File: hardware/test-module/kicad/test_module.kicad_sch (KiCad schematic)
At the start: 13 parts, among them J1 Barrel_Jack_12V, M1 ERM_Motor, M2 Stepper_4wire, M3 Servo_3pin, U1 D24V22F5_Buck, U2 Pi_Pico, U3 DRV2605L_Breakout, U4 DRV8871_Breakout, U5 DRV8825_Carrier

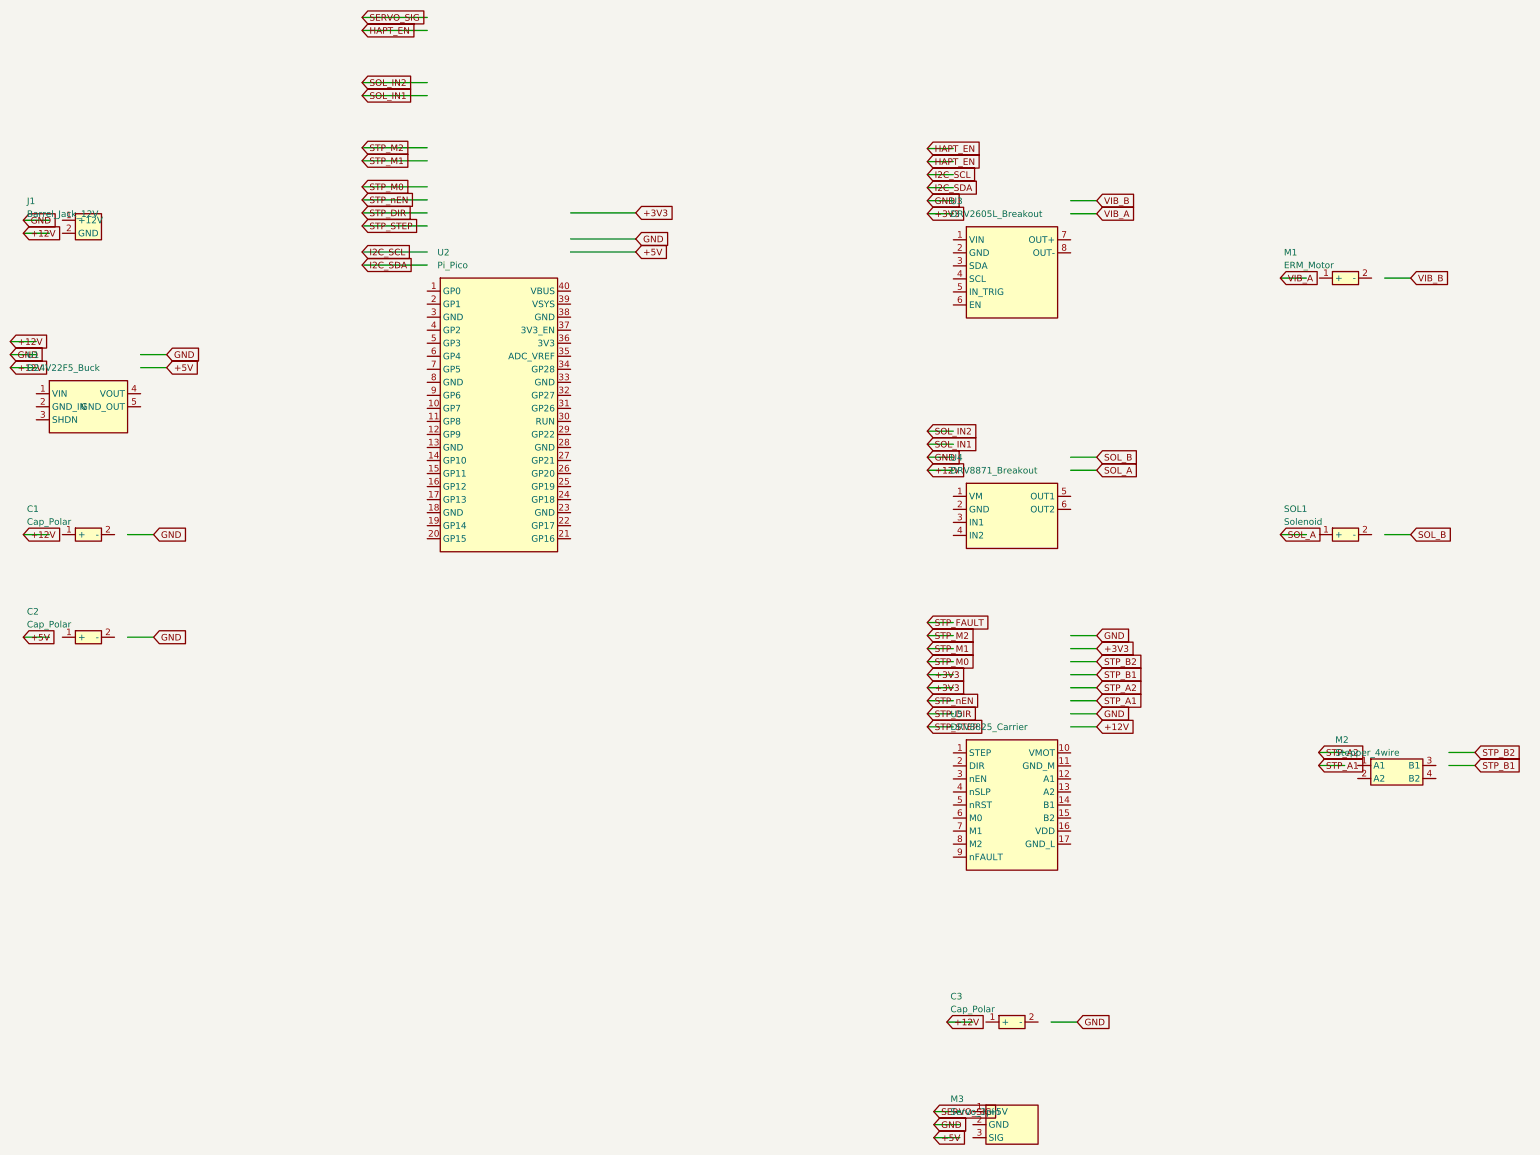
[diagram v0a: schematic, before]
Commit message: Address PR review: smooth servo, Pico W, fix schematic alignment, add shunt regulator
Agent-Logs-Url: https://github.com/vertical-cloud-lab/powder-doser/sessions/35e0fe52-25cf-4560-81b1-879b81744dff

Co-authored-by: swcharles <185848910+swcharles@users.noreply.github.com>
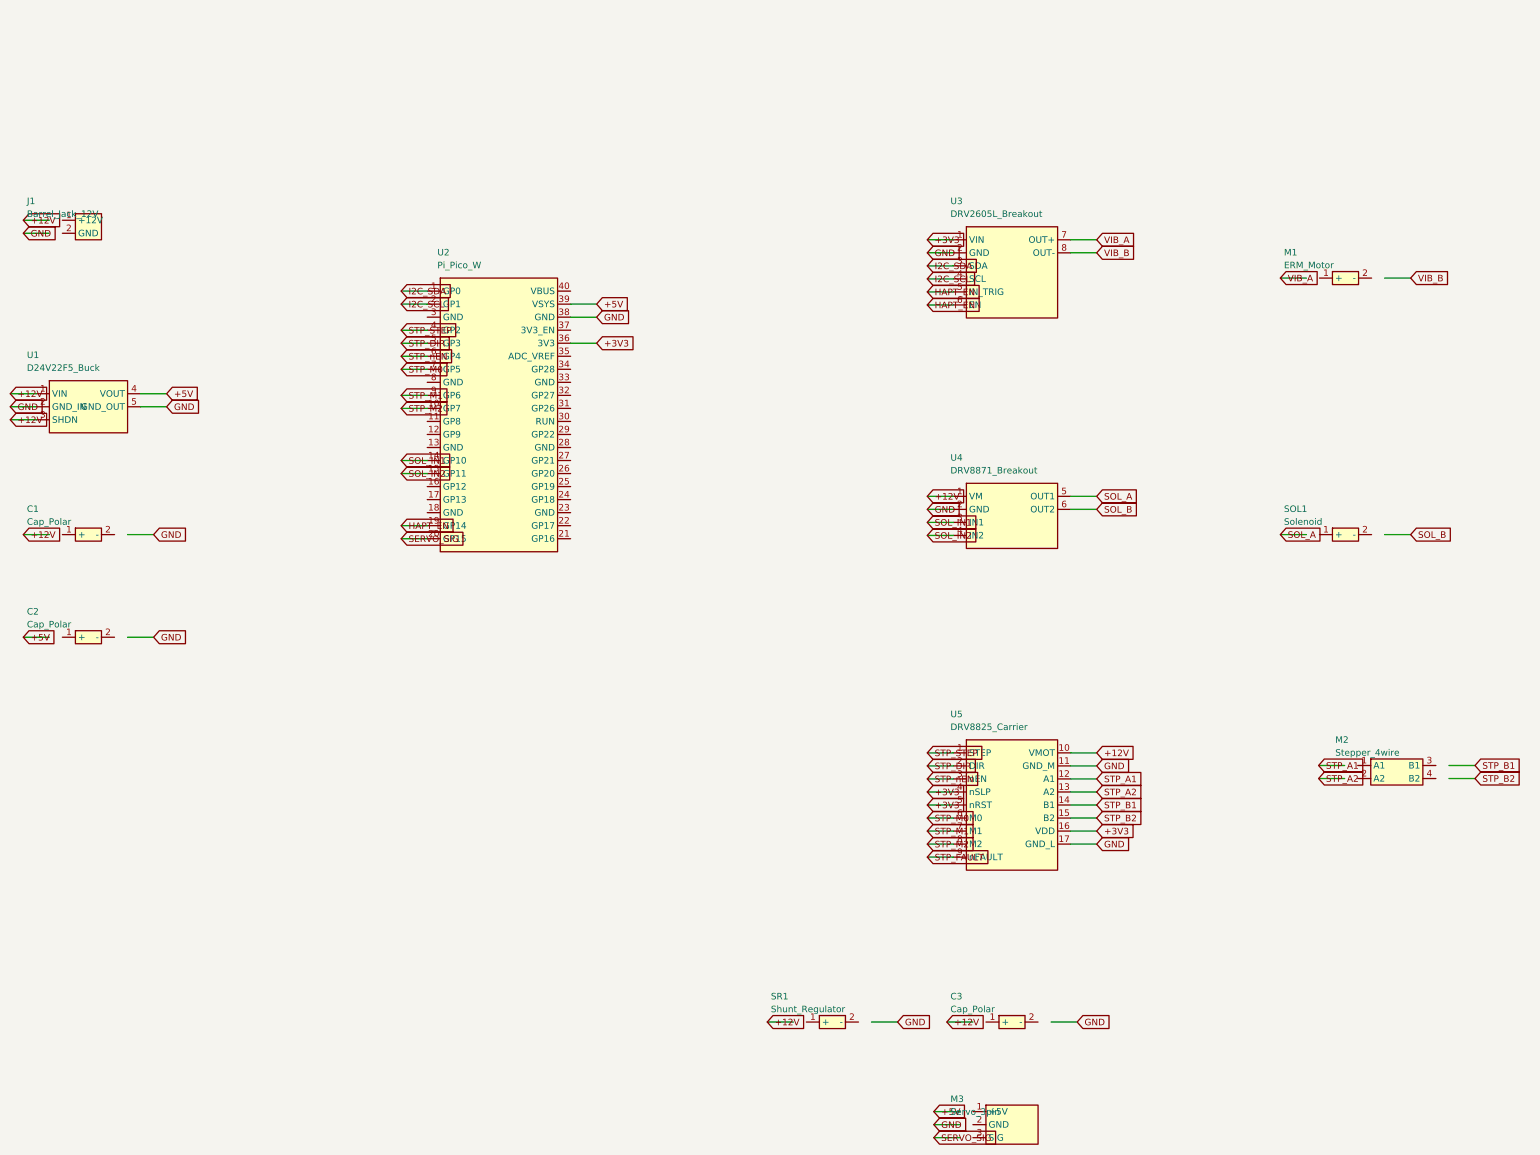
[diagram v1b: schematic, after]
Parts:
- removed U2: Pi_Pico, symbol test_module:Pi_Pico
- added SR1: Shunt_Regulator, symbol test_module:Shunt_Regulator
- added U2: Pi_Pico_W, symbol test_module:Pi_Pico_W
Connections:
- net +12V: now also U1.1 (VIN), U1.3 (SHDN), U4.1 (VM), U5.10 (VMOT)
- net +3V3: now also U3.1 (VIN), U5.16 (VDD), U5.4 (nSLP), U5.5 (nRST), U2.36 (3V3)
- net +5V: now also U1.4 (VOUT), U2.39 (VSYS)
- net GND: now also U1.2 (GND_IN), U1.5 (GND_OUT), U3.2 (GND), U4.2 (GND), U5.11 (GND_M), U5.17 (GND_L), U2.38 (GND)
- net HAPT_EN: now also U3.5 (IN_TRIG), U3.6 (EN), U2.19 (GP14)
- net I2C_SCL: now also U3.4 (SCL), U2.2 (GP1)
- net I2C_SDA: now also U3.3 (SDA), U2.1 (GP0)
- net SERVO_SIG: now also U2.20 (GP15)
- net SOL_A: now also U4.5 (OUT1)
- net SOL_B: now also U4.6 (OUT2)
- net SOL_IN1: now also U4.3 (IN1), U2.14 (GP10)
- net SOL_IN2: now also U4.4 (IN2), U2.15 (GP11)
- net STP_A1: now also U5.12 (A1)
- net STP_A2: now also U5.13 (A2)
- net STP_B1: now also U5.14 (B1)
- net STP_B2: now also U5.15 (B2)
- net STP_DIR: now also U5.2 (DIR), U2.5 (GP3)
- net STP_FAULT: now also U5.9 (nFAULT)
- net STP_M0: now also U5.6 (M0), U2.7 (GP5)
- net STP_M1: now also U5.7 (M1), U2.9 (GP6)
- net STP_M2: now also U5.8 (M2), U2.10 (GP7)
- net STP_STEP: now also U5.1 (STEP), U2.4 (GP2)
- net STP_nEN: now also U5.3 (nEN), U2.6 (GP4)
- net VIB_A: now also U3.7 (OUT+)
- net VIB_B: now also U3.8 (OUT-)

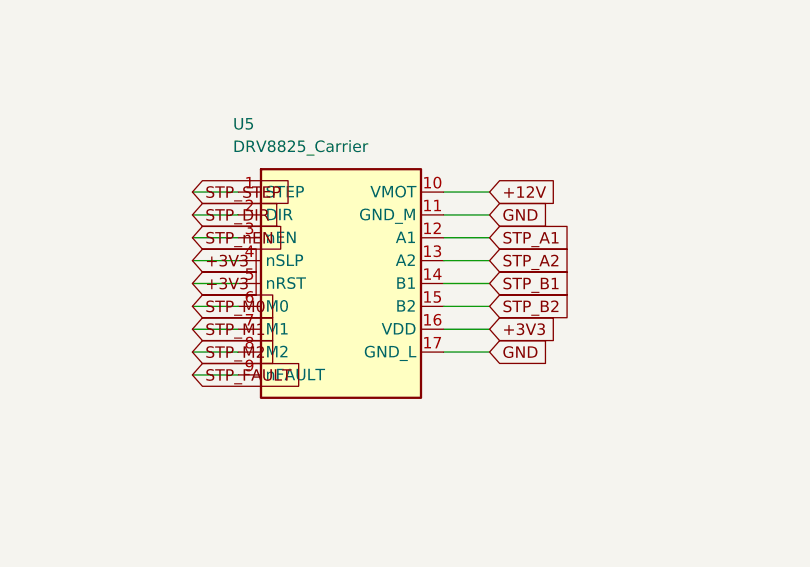
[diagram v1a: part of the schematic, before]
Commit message: DRV8825: 8-pin Pololu #2133 layout (no VDD); document Tic T500 omission
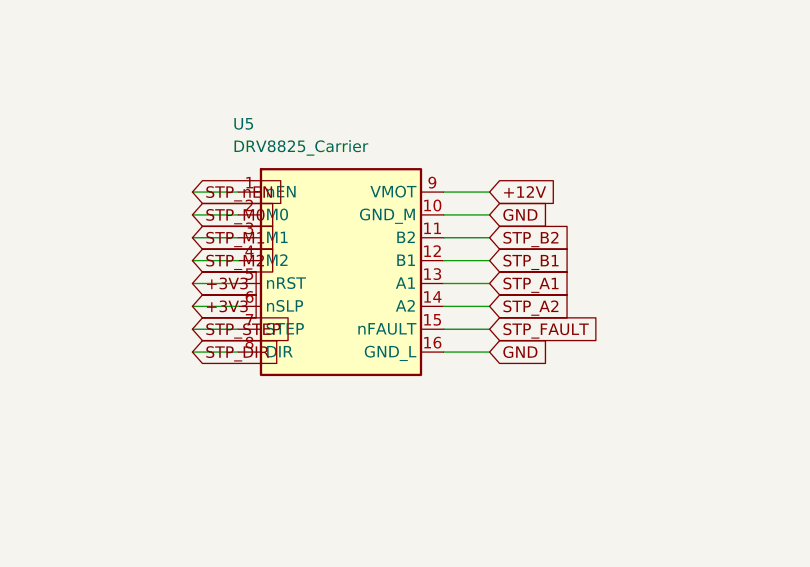
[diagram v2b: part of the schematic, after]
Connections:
- net +12V: now also U5.9 (VMOT); no longer U5.10 (VMOT)
- net +3V3: now also U5.6 (nSLP); no longer U5.16 (VDD), U5.4 (nSLP)
- net GND: now also U5.10 (GND_M), U5.16 (GND_L); no longer U5.11 (GND_M), U5.17 (GND_L)
- net STP_A1: now also U5.13 (A1); no longer U5.12 (A1)
- net STP_A2: now also U5.14 (A2); no longer U5.13 (A2)
- net STP_B1: now also U5.12 (B1); no longer U5.14 (B1)
- net STP_B2: now also U5.11 (B2); no longer U5.15 (B2)
- net STP_DIR: now also U5.8 (DIR); no longer U5.2 (DIR)
- net STP_FAULT: now also U5.15 (nFAULT); no longer U5.9 (nFAULT)
- net STP_M0: now also U5.2 (M0); no longer U5.6 (M0)
- net STP_M1: now also U5.3 (M1); no longer U5.7 (M1)
- net STP_M2: now also U5.4 (M2); no longer U5.8 (M2)
- net STP_STEP: now also U5.7 (STEP); no longer U5.1 (STEP)
- net STP_nEN: now also U5.1 (nEN); no longer U5.3 (nEN)
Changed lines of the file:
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@@
   )
+)
+(wire (pts (xy 198.57 157.78) (xy 193.48999999999998 157.78))
+  (stroke (width 0) (type default)) (stroke (width 0) (type default))
+)
+(global_label "STP_STEP" (shape input) (at 193.48999999999998 157.78 180) (fields_autoplaced)
+  (effects (font (size 1.27 1.27)) (justify left))
+)
+(wire (pts (xy 198.57 160.32) (xy 193.48999999999998 160.32))
+  (stroke (width 0) (type default)) (stroke (width 0) (type default))
+)
+(global_label "STP_DIR" (shape input) (at 193.48999999999998 160.32 180) (fields_autoplaced)
+  (effects (font (size 1.27 1.27)) (justify left))
 )
 (wire (pts (xy 198.57 142.54) (xy 193.48999999999998 142.54))
   (stroke (width 0) (type default)) (stroke (width 0) (type default))
 )
-(global_label "STP_STEP" (shape input) (at 193.48999999999998 142.54 180) (fields_autoplaced)
+(global_label "STP_nEN" (shape input) (at 193.48999999999998 142.54 180) (fields_autoplaced)
   (effects (font (size 1.27 1.27)) (justify left))
 )
-(wire (pts (xy 198.57 145.08) (xy 193.48999999999998 145.08))
+(wire (pts (xy 198.57 155.24) (xy 193.48999999999998 155.24))
   (stroke (width 0) (type default)) (stroke (width 0) (type default))
 )
-(global_label "STP_DIR" (shape input) (at 193.48999999999998 145.08 180) (fields_autoplaced)
-  (effects (font (size 1.27 1.27)) (justify left))
-)
-(wire (pts (xy 198.57 147.62) (xy 193.48999999999998 147.62))
-  (stroke (width 0) (type default)) (stroke (width 0) (type default))
-)
-(global_label "STP_nEN" (shape input) (at 193.48999999999998 147.62 180) (fields_autoplaced)
-  (effects (font (size 1.27 1.27)) (justify left))
-)
-(wire (pts (xy 198.57 150.16) (xy 193.48999999999998 150.16))
-  (stroke (width 0) (type default)) (stroke (width 0) (type default))
-)
-(global_label "+3V3" (shape input) (at 193.48999999999998 150.16 180) (fields_autoplaced)
+(global_label "+3V3" (shape input) (at 193.48999999999998 155.24 180) (fields_autoplaced)
   (effects (font (size 1.27 1.27)) (justify left))
 )
@@
   (effects (font (size 1.27 1.27)) (justify left))
 )
-(wire (pts (xy 198.57 155.24) (xy 193.48999999999998 155.24))
+(wire (pts (xy 198.57 145.08) (xy 193.48999999999998 145.08))
   (stroke (width 0) (type default)) (stroke (width 0) (type default))
 )
-(global_label "STP_M0" (shape input) (at 193.48999999999998 155.24 180) (fields_autoplaced)
+(global_label "STP_M0" (shape input) (at 193.48999999999998 145.08 180) (fields_autoplaced)
   (effects (font (size 1.27 1.27)) (justify left))
 )
-(wire (pts (xy 198.57 157.78) (xy 193.48999999999998 157.78))
+(wire (pts (xy 198.57 147.62) (xy 193.48999999999998 147.62))
   (stroke (width 0) (type default)) (stroke (width 0) (type default))
 )
-(global_label "STP_M1" (shape input) (at 193.48999999999998 157.78 180) (fields_autoplaced)
+(global_label "STP_M1" (shape input) (at 193.48999999999998 147.62 180) (fields_autoplaced)
   (effects (font (size 1.27 1.27)) (justify left))
 )
-(wire (pts (xy 198.57 160.32) (xy 193.48999999999998 160.32))
+(wire (pts (xy 198.57 150.16) (xy 193.48999999999998 150.16))
   (stroke (width 0) (type default)) (stroke (width 0) (type default))
 )
-(global_label "STP_M2" (shape input) (at 193.48999999999998 160.32 180) (fields_autoplaced)
+(global_label "STP_M2" (shape input) (at 193.48999999999998 150.16 180) (fields_autoplaced)
   (effects (font (size 1.27 1.27)) (justify left))
 )
-(wire (pts (xy 198.57 162.86) (xy 193.48999999999998 162.86))
+(wire (pts (xy 221.43 157.78) (xy 226.51000000000002 157.78))
   (stroke (width 0) (type default)) (stroke (width 0) (type default))
 )
-(global_label "STP_FAULT" (shape input) (at 193.48999999999998 162.86 180) (fields_autoplaced)
+(global_label "STP_FAULT" (shape input) (at 226.51000000000002 157.78 0) (fields_autoplaced)
   (effects (font (size 1.27 1.27)) (justify left))
 )
@@
   (effects (font (size 1.27 1.27)) (justify left))
 )
-(wire (pts (xy 221.43 157.78) (xy 226.51000000000002 157.78))
-  (stroke (width 0) (type default)) (stroke (width 0) (type default))
-)
-(global_label "+3V3" (shape input) (at 226.51000000000002 157.78 0) (fields_autoplaced)
-  (effects (font (size 1.27 1.27)) (justify left))
-)
 (wire (pts (xy 221.43 160.32) (xy 226.51000000000002 160.32))
   (stroke (width 0) (type default)) (stroke (width 0) (type default))
@@
   (effects (font (size 1.27 1.27)) (justify left))
 )
-(wire (pts (xy 221.43 147.62) (xy 226.51000000000002 147.62))
+(wire (pts (xy 221.43 152.7) (xy 226.51000000000002 152.7))
   (stroke (width 0) (type default)) (stroke (width 0) (type default))
 )
-(global_label "STP_A1" (shape input) (at 226.51000000000002 147.62 0) (fields_autoplaced)
+(global_label "STP_A1" (shape input) (at 226.51000000000002 152.7 0) (fields_autoplaced)
+  (effects (font (size 1.27 1.27)) (justify left))
+)
+(wire (pts (xy 221.43 155.24) (xy 226.51000000000002 155.24))
+  (stroke (width 0) (type default)) (stroke (width 0) (type default))
+)
+(global_label "STP_A2" (shape input) (at 226.51000000000002 155.24 0) (fields_autoplaced)
   (effects (font (size 1.27 1.27)) (justify left))
 )
@@
   (stroke (width 0) (type default)) (stroke (width 0) (type default))
 )
-(global_label "STP_A2" (shape input) (at 226.51000000000002 150.16 0) (fields_autoplaced)
+(global_label "STP_B1" (shape input) (at 226.51000000000002 150.16 0) (fields_autoplaced)
   (effects (font (size 1.27 1.27)) (justify left))
 )
-(wire (pts (xy 221.43 152.7) (xy 226.51000000000002 152.7))
+(wire (pts (xy 221.43 147.62) (xy 226.51000000000002 147.62))
   (stroke (width 0) (type default)) (stroke (width 0) (type default))
 )
-(global_label "STP_B1" (shape input) (at 226.51000000000002 152.7 0) (fields_autoplaced)
+(global_label "STP_B2" (shape input) (at 226.51000000000002 147.62 0) (fields_autoplaced)
   (effects (font (size 1.27 1.27)) (justify left))
 )
-(wire (pts (xy 221.43 155.24) (xy 226.51000000000002 155.24))
-  (stroke (width 0) (type default)) (stroke (width 0) (type default))
-)
-(global_label "STP_B2" (shape input) (at 226.51000000000002 155.24 0) (fields_autoplaced)
-  (effects (font (size 1.27 1.27)) (justify left))
-)
